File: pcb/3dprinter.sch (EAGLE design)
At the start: 123 parts, among them IC1 NRF51822, IC1_REG REGULATOR, IC2_REG LP2985-3V3, Q1_BED MOSFET, Q1_FAN1 MOSFETSOT23, Q1_FAN2 MOSFETSOT23, Q1_NOZ MOSFET, Y1 CRYSTAL

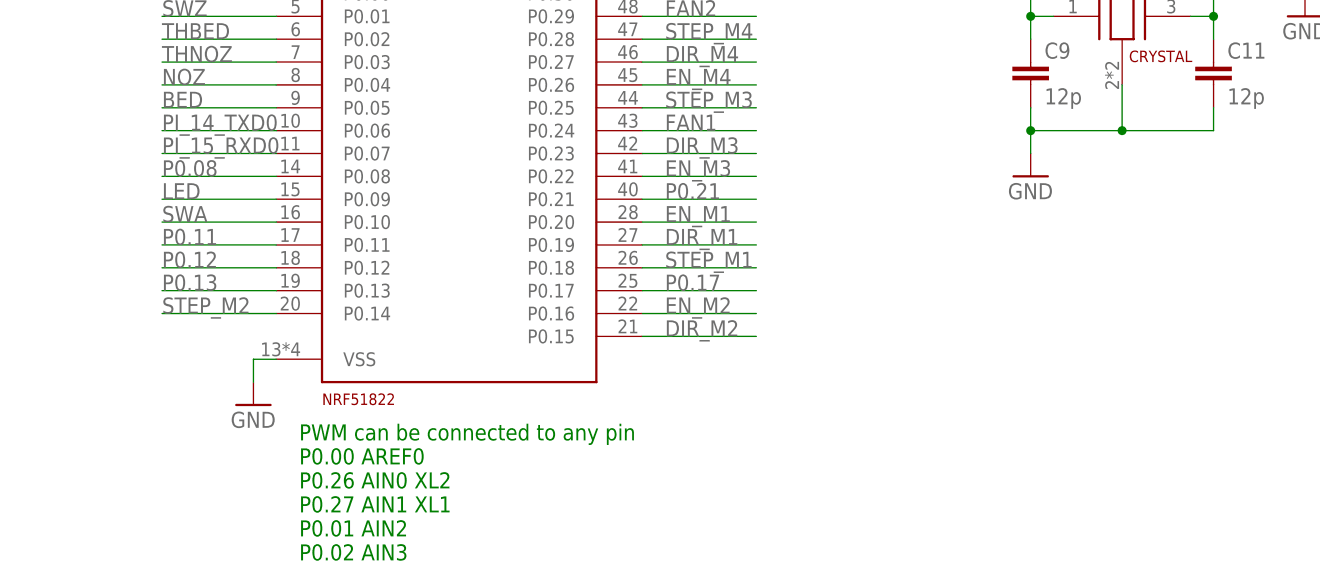
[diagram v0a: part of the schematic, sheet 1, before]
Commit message: Added testpads ERC/DRC OK
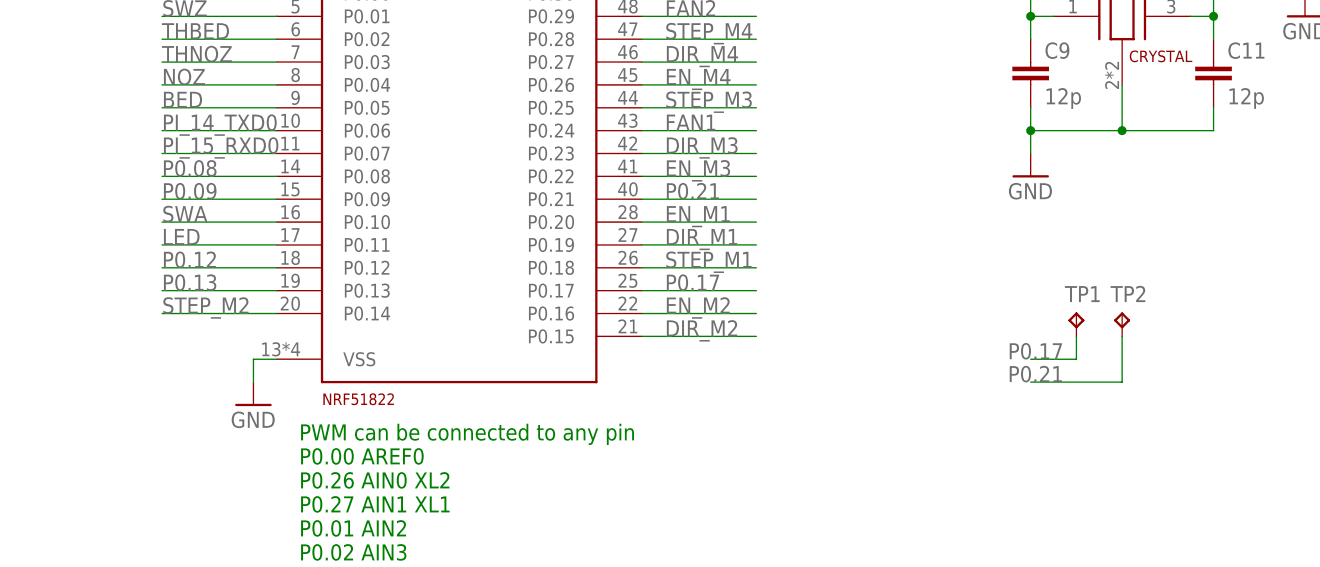
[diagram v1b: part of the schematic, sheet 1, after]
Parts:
- added TP1, TP2: TPB1,27, 3dprinter:TPB1,27
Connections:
- removed net P0.11: IC1.P0.11
- new net P0.09: IC1.P0.09
- net LED: now also IC1.P0.11; no longer IC1.P0.09
- net P0.17: now also TP1.TP
- net P0.21: now also TP2.TP
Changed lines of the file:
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@@
 <part name="R1_LED" library="3dprinter" deviceset="R-US_" device="R0603" value="100R"/>
 <part name="GND39" library="supply" deviceset="GND" device=""/>
+<part name="TP1" library="3dprinter" deviceset="TP" device="B1,27"/>
+<part name="TP2" library="3dprinter" deviceset="TP" device="B1,27"/>
 </parts>
 <sheets>
@@
 <instance part="R1_LED" gate="G$1" x="205.74" y="238.76" rot="R270"/>
 <instance part="GND39" gate="1" x="205.74" y="218.44"/>
+<instance part="TP1" gate="G$1" x="248.92" y="111.76"/>
+<instance part="TP2" gate="G$1" x="254" y="111.76"/>
 </instances>
 <busses>
@@
 </segment>
 </net>
-<net name="P0.11" class="0">
-<segment>
-<pinref part="IC1" gate="G$1" pin="P0.11"/>
-<wire x1="160.02" y1="119.38" x2="147.32" y2="119.38" width="0.1524" layer="91"/>
-<label x="147.32" y="119.38" size="1.778" layer="95"/>
-</segment>
-</net>
 <net name="P0.12" class="0">
 <segment>
@@
 <label x="203.2" y="124.46" size="1.778" layer="95"/>
 </segment>
+<segment>
+<pinref part="TP2" gate="G$1" pin="TP"/>
+<wire x1="254" y1="109.22" x2="254" y2="104.14" width="0.1524" layer="91"/>
+<wire x1="254" y1="104.14" x2="243.84" y2="104.14" width="0.1524" layer="91"/>
+<label x="241.3" y="104.14" size="1.778" layer="95"/>
+</segment>
 </net>
 <net name="EN_M4" class="0">
@@
 <wire x1="213.36" y1="114.3" x2="200.66" y2="114.3" width="0.1524" layer="91"/>
 <label x="203.2" y="114.3" size="1.778" layer="95"/>
+</segment>
+<segment>
+<pinref part="TP1" gate="G$1" pin="TP"/>
+<wire x1="248.92" y1="109.22" x2="248.92" y2="106.68" width="0.1524" layer="91"/>
+<wire x1="248.92" y1="106.68" x2="243.84" y2="106.68" width="0.1524" layer="91"/>
+<label x="241.3" y="106.68" size="1.778" layer="95"/>
 </segment>
 </net>
@@
 <wire x1="205.74" y1="248.92" x2="198.12" y2="248.92" width="0.1524" layer="91"/>
 </segment>
+<segment>
+<pinref part="IC1" gate="G$1" pin="P0.11"/>
+<wire x1="160.02" y1="119.38" x2="147.32" y2="119.38" width="0.1524" layer="91"/>
+<label x="147.32" y="119.38" size="1.778" layer="95"/>
+</segment>
+</net>
+<net name="P0.09" class="0">
 <segment>
 <pinref part="IC1" gate="G$1" pin="P0.09"/>
@@
 </sheet>
 </sheets>
+<errors>
+</errors>
 </schematic>
 </drawing>

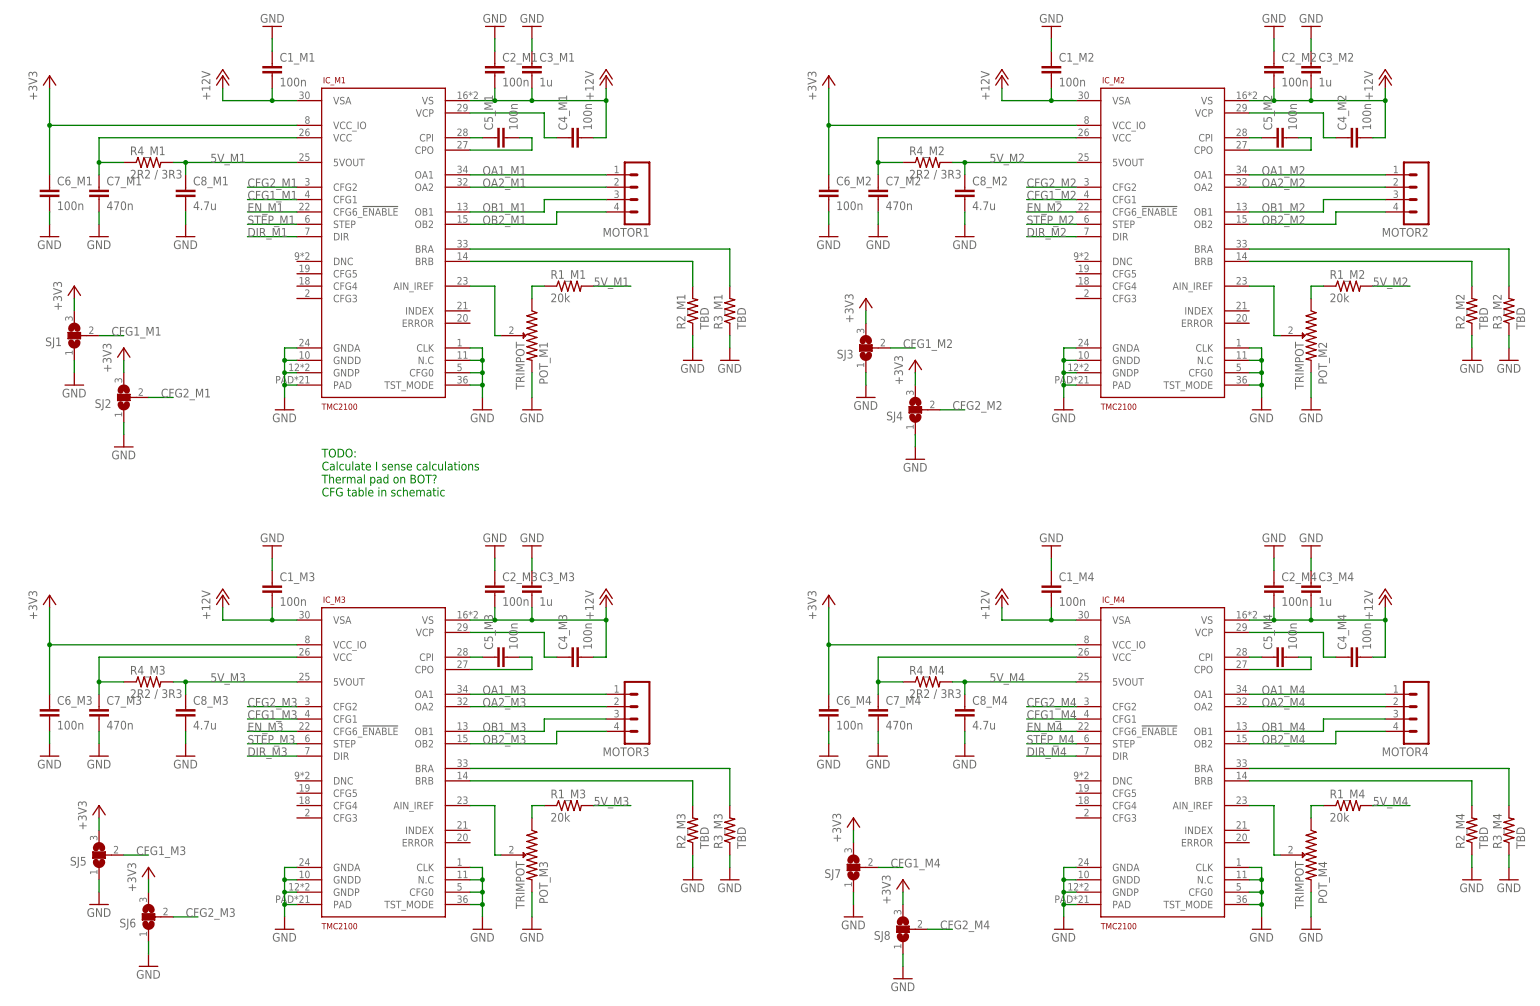
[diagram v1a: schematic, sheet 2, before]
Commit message: Top/Bot silkscreen and clearance
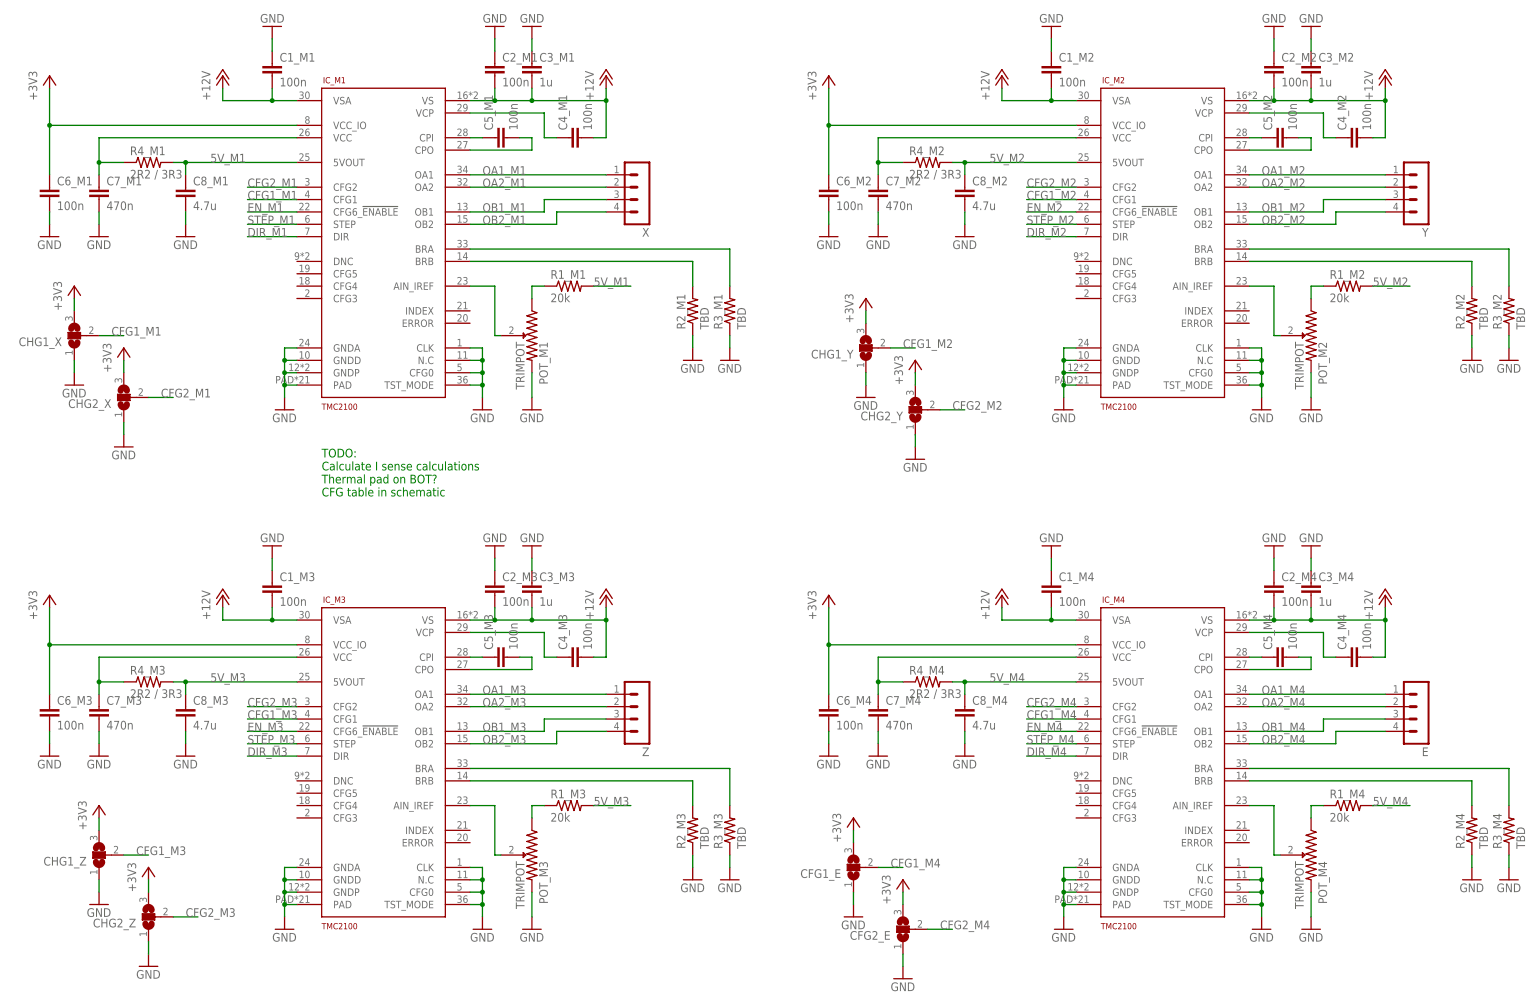
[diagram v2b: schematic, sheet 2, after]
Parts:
- renumbered MOTOR1 to X, MOTOR2 to Y, MOTOR3 to Z, MOTOR4 to E, NOZ to NOZZLE, SJ1 to CHG1_X, SJ2 to CHG2_X, SJ3 to CHG1_Y, SJ4 to CHG2_Y, SJ5 to CHG1_Z, SJ6 to CHG2_Z, SJ7 to CFG1_E, SJ8 to CFG2_E, SWX to END_X, SWY to END_Y, SWZ to END_Z, TH_BED to TEMP_BED, TH_NOZ to TEMP_NOZZLE, TP1 to P0.17, TP2 to P0.21
